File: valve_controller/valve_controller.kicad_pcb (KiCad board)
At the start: 2 copper layers, 34 parts, among them J1 643260100604, J10 643260100604, J11 643260100604, J2 T4143512051-000, J3 M12A-04PMMP-SF8001, J5 643260100604, J6 643260100604, J7 643260100604, J8 643260100604, J9 643260100604, U1 LAN8720A, U2 ADS1115IDGS, U3 MCP4728, U4 ESP32-WROOM-32, U5 LM2596S-5, U7 ADS1115IDGS, U8 MCP4728, U9 AP2112K-3.3, Y2 ASE-25.000MHZ-LC-T

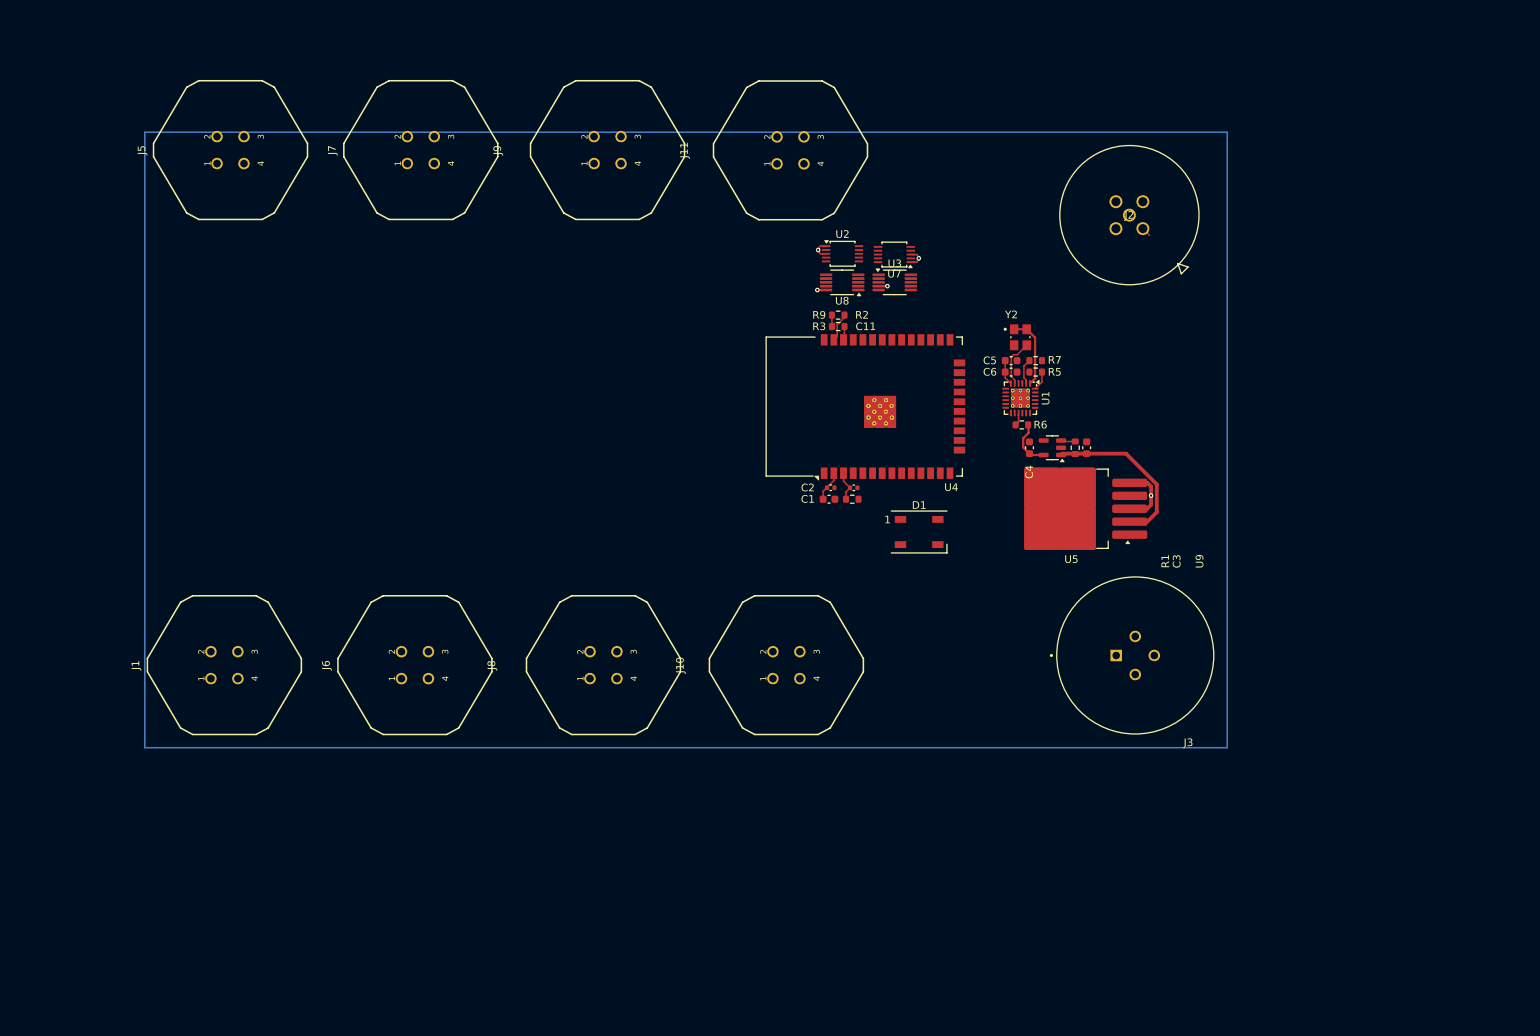
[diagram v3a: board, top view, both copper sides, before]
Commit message: Added 12v power bus
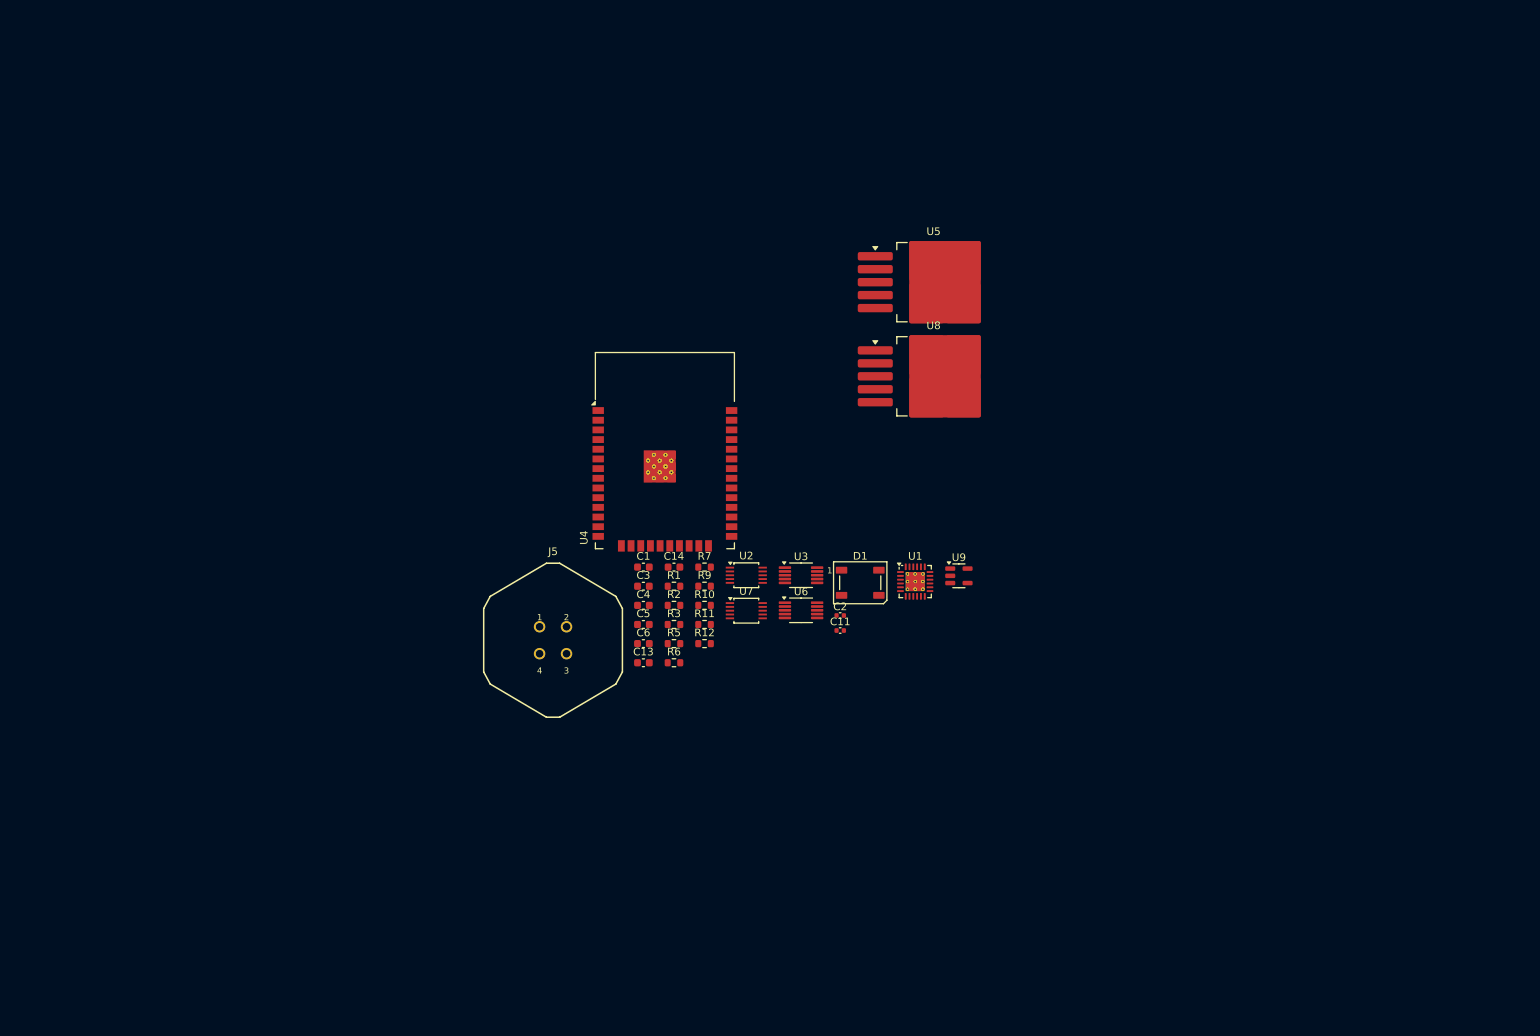
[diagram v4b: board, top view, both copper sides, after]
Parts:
- removed J1, J10, J11, J6, J7, J8, J9: 643260100604, 643260100604:643260100604
- removed J2: T4143512051-000, T4143512051_000:CONN5_T4143512051
- removed J3: M12A-04PMMP-SF8001, M12A-04PMMP-SF8001:AMPHENOL_M12A-04PMMP-SF8001
- removed Y2: ASE-25.000MHZ-LC-T, ASE-25.000MHZ-LC-T:XTAL_ASE-25.000MHZ-LC-T
- added C13: 10uF, Capacitor_SMD:C_0603_1608Metric, F.Cu at (120.5, 122.5)
- added C14: 0.1uF, Capacitor_SMD:C_0603_1608Metric, F.Cu at (124.5, 109.9)
- added R10: 10k, Resistor_SMD:R_0603_1608Metric, F.Cu at (128.5, 114.9)
- added R11: 10k, Resistor_SMD:R_0603_1608Metric, F.Cu at (128.5, 117.4)
- added R12: 100k, Resistor_SMD:R_0603_1608Metric, F.Cu at (128.5, 119.9)
- added U6: GP8403, Package_SO:MSOP-10_3x3mm_P0.5mm, F.Cu at (141.2, 115.6)
- U5: value LM2596S-5 -> LM2576S-12
- U8: value MCP4728 -> LM2576S-5; footprint Package_SO:MSOP-10_3x3mm_P0.5mm -> Package_TO_SOT_SMD:TO-263-5_TabPin3
- moved J5 77.0 mm to (108.6, 119.5), turned to 0 degrees
- moved C3 60.9 mm to (120.5, 112.4), turned to 0 degrees
- moved C6 60.0 mm to (120.5, 119.9)
- moved C5 59.4 mm to (120.5, 117.4)
- moved R5 59.3 mm to (124.5, 119.9)
- moved R1 55.7 mm to (124.5, 112.4), turned to 0 degrees
- moved R6 55.3 mm to (124.5, 122.5)
- moved C4 54.7 mm to (120.5, 114.9), turned to 0 degrees
- moved R7 51.2 mm to (128.5, 109.9)
- moved U7 50.6 mm to (134.0, 115.6), turned to 0 degrees
- moved R3 44.6 mm to (124.5, 117.4)
- moved U2 44.0 mm to (134.0, 111.0)
- moved U3 40.3 mm to (141.2, 111.0)
- moved R9 39.7 mm to (128.5, 112.4)
- moved U5 34.8 mm to (158.5, 72.5), turned to 0 degrees
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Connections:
- J5 pad 1: /AIN0_ADC0 -> +24V
- J5 pad 2: unconnected-(J5-Pad2) -> /ANOUT0_DAC0
- J5 pad 3: unconnected-(J5-Pad3) -> GND
- J5 pad 4: /ANOUT0_DAC0 -> /AIN0_ADC0
- U2 pad 1: GND -> /SCL
- U3 pad 1: +3V3 -> +5V
- U3 pad 4: GND -> /nLDAC_DAC0
- U3 pad 5: unconnected-(U3-RDY/~{BSY}-Pad5) -> /RDY_DAC0
- U4 pad 10: unconnected-(U4-IO25-Pad10) -> /RGB_LED
- U4 pad 11: unconnected-(U4-IO26-Pad11) -> /RDY_DAC0
- U4 pad 12: unconnected-(U4-IO27-Pad12) -> /nLDAC_DAC0
- U4 pad 34: unconnected-(U4-RXD0/IO3-Pad34) -> /ESP_TX
- U4 pad 35: unconnected-(U4-TXD0/IO1-Pad35) -> /ESP_RX
- U4 pad 6: unconnected-(U4-IO34-Pad6) -> /RXD1
- U4 pad 7: unconnected-(U4-IO35-Pad7) -> /RXD0
- U4 pad 8: unconnected-(U4-IO32-Pad8) -> /MDC
- U5 pad 1: +24V -> unconnected-(U5-VIN-Pad1)
- U5 pad 2: +5V -> unconnected-(U5-OUT-Pad2)
- U5 pad 3: GND -> unconnected-(U5-GND-Pad3)
- U5 pad 5: GND -> unconnected-(U5-~{ON}/OFF-Pad5)
- U7 pad 1: GND -> /SDA
- U8 pad 1: +3V3 -> unconnected-(U8-VIN-Pad1)
- U8 pad 2: /SCL -> unconnected-(U8-OUT-Pad2)
- U8 pad 3: /SDA -> unconnected-(U8-GND-Pad3)
- U8 pad 4: GND -> unconnected-(U8-FB-Pad4)
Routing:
- net +5V: track 22.0 -> 0.00 mm
- net +3V3: track 21.9 -> 0.00 mm
- net GND: track 16.3 -> 0.00 mm, vias 5 -> 0
- net /25MHZ: track 6.32 -> 0.00 mm
- net /ESP_EN: track 3.99 -> 0.00 mm
- net /SDA: track 3.82 -> 0.00 mm
- net Net-(U1-LED2/~{INTSEL}): track 3.41 -> 0.00 mm
- net Net-(U1-VDDCR): track 3.30 -> 0.00 mm
- net Net-(U1-RBIAS): track 2.55 -> 0.00 mm
- net Net-(U9-EN): track 1.91 -> 0.00 mm
- net /SCL: track 1.80 -> 0.00 mm
- net Net-(U1-~{RST}): track 1.72 -> 0.00 mm
- net unconnected-(U4-IO34-Pad6): track 0.53 -> 0.00 mm
- net /TXD0: track 0.53 -> 0.00 mm

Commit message: Layout V2
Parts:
- removed R10, R11: 10k, Resistor_SMD:R_0603_1608Metric
- removed R12, R9: 100k, Resistor_SMD:R_0603_1608Metric
- added C10: 100uF, Capacitor_SMD:C_0603_1608Metric, F.Cu at (184.5, 95.7)
- added C12: 1uF, Capacitor_SMD:C_0603_1608Metric, F.Cu at (93.1, 85.0)
- added C15: 10uF, Capacitor_SMD:C_0603_1608Metric, F.Cu at (154.9, 83.7)
- added C16: 10uF, Capacitor_SMD:C_0603_1608Metric, F.Cu at (96.1, 85.0)
- added C17: 10uF, Capacitor_SMD:C_0603_1608Metric, F.Cu at (156.4, 83.7)
- added C18: 100uF, Capacitor_SMD:C_0603_1608Metric, F.Cu at (197.6, 68.6)
- added C19: 100uF, Capacitor_SMD:C_0603_1608Metric, F.Cu at (196.7, 82.2)
- added C20: 1uF, Capacitor_SMD:C_0603_1608Metric, F.Cu at (96.4, 108.5)
- added C21: 1uF, Capacitor_SMD:C_0603_1608Metric, F.Cu at (153.3, 109.8)
- added C22: 10uF, Capacitor_SMD:C_0603_1608Metric, F.Cu at (93.4, 108.5)
- added C23: 10uF, Capacitor_SMD:C_0603_1608Metric, F.Cu at (156.2, 109.8)
- added C24: 22uF, Capacitor_SMD:C_0603_1608Metric, F.Cu at (167.1, 99.6)
- added C25: 10uF, Capacitor_SMD:C_0603_1608Metric, F.Cu at (94.9, 108.5)
- added C26: 10uF, Capacitor_SMD:C_0603_1608Metric, F.Cu at (154.8, 109.8)
- added C27: 22uF, Capacitor_SMD:C_0603_1608Metric, F.Cu at (175.9, 100.4)
- added C7: 100uF, Capacitor_SMD:C_0603_1608Metric, F.Cu at (198.4, 106.3)
- added C8: 10nF, Capacitor_SMD:C_0603_1608Metric, F.Cu at (171.8, 82.0)
- added C9: 270pF, Capacitor_SMD:C_0603_1608Metric, F.Cu at (176.4, 84.0)
- added D10: SMAJ12A, Diode_SMD:D_SMA, F.Cu at (88.8, 113.8)
- added D11: SMAJ12A, Diode_SMD:D_SMA, F.Cu at (148.7, 114.2)
- added D2: SS34, Diode_SMD:D_SMA, F.Cu at (195.9, 94.9)
- added D3: SMAJ12A, Diode_SMD:D_SMA, F.Cu at (100.8, 79.5)
- added D4: SMAJ12A, Diode_SMD:D_SMA, F.Cu at (160.6, 79.3)
- added D5: SMAJ12A, Diode_SMD:D_SMA, F.Cu at (89.0, 79.4)
- added D6: SMAJ12A, Diode_SMD:D_SMA, F.Cu at (149.3, 79.2)
- added D7: SS34, Diode_SMD:D_SMA, F.Cu at (185.3, 81.5)
- added D8: SMAJ12A, Diode_SMD:D_SMA, F.Cu at (100.5, 113.7)
- added D9: SMAJ12A, Diode_SMD:D_SMA, F.Cu at (160.1, 113.8)
- added J1: T4132512041-000, T4132512041-000:CONN4_T4132512041, F.Cu at (217.0, 66.5)
- added J10: M12A-05PFFP-SF8001, M12A_05footprints:CONN_SF8001_AMP, F.Cu at (139.4, 121.8)
- added J11: M12A-05PFFP-SF8001, M12A_05footprints:CONN_SF8001_AMP, F.Cu at (169.4, 121.8)
- added J2: 20021511-00006T4LF, 20021511_00006T4LF:AMPHENOL_20021511-00006T4LF, F.Cu at (191.9, 124.3)
- added J3: 54-00384, 54_00384:54, F.Cu at (214.4, 124.2)
- added J4: M12A-05PFFP-SF8001, M12A_05footprints:CONN_SF8001_AMP, F.Cu at (79.4, 66.8)
- added J6: M12A-05PFFP-SF8001, M12A_05footprints:CONN_SF8001_AMP, F.Cu at (139.4, 66.7)
- added J7: M12A-05PFFP-SF8001, M12A_05footprints:CONN_SF8001_AMP, F.Cu at (169.4, 66.7)
- added J8: M12A-05PFFP-SF8001, M12A_05footprints:CONN_SF8001_AMP, F.Cu at (79.4, 121.7)
- added J9: M12A-05PFFP-SF8001, M12A_05footprints:CONN_SF8001_AMP, F.Cu at (109.4, 121.7)
- added L1: SRP6530A-100M, SRP6530A_100M:IND_SRP6530A_BRN, F.Cu at (189.9, 94.5)
- added L2: SRP6530A-100M, SRP6530A_100M:IND_SRP6530A_BRN, F.Cu at (191.4, 82.0)
- added R4: 12.1k, Resistor_SMD:R_0603_1608Metric, F.Cu at (175.6, 93.4)
- added U10: GP8403-TC50-EW, GP8403:ESSOP-10_L4.9-W3.9-P1.00-LS6.0-BL-EP, F.Cu at (154.8, 102.9)
- added U11: AP2112K-3.3, Package_TO_SOT_SMD:SOT-23-5, F.Cu at (171.6, 100.4)
- added Y1: ASE-25.000MHZ-LC-T, ASE-25.000MHZ-LC-T:XTAL_ASE-25.000MHZ-LC-T, F.Cu at (175.6, 89.0)
- C11: value 0.1uF -> 100nF; footprint Capacitor_SMD:C_0402_1005Metric -> Capacitor_SMD:C_0603_1608Metric
- C13: value 10uF -> 1uF
- C14: value 0.1uF -> 10uF
- C2: footprint Capacitor_SMD:C_0402_1005Metric -> Capacitor_SMD:C_0603_1608Metric
- C3: value 22uF -> 0.1uF
- C4: value 22uF -> 10nF
- C5: value 1uF -> 22nF
- C6: value 470pF -> 1uF
- J5: value 643260100604 -> M12A-05PFFP-SF8001; footprint 643260100604:643260100604 -> M12A_05footprints:CONN_SF8001_AMP
- R1, R3: value 100k -> 10k
- R5: value 12.1k -> 100k
- R6, R7: value 10k -> 100k
- U2: value ADS1115IDGS -> ESP32-WROOM-32; footprint Package_SO:TSSOP-10_3x3mm_P0.5mm -> RF_Module:ESP32-WROOM-32
- U3: value MCP4728 -> LM2576S-12; footprint Package_SO:MSOP-10_3x3mm_P0.5mm -> Package_TO_SOT_SMD:TO-263-5_TabPin3
- U4: value ESP32-WROOM-32 -> ADS1115IDGS; footprint RF_Module:ESP32-WROOM-32 -> Package_SO:TSSOP-10_3x3mm_P0.5mm
- U5: value LM2576S-12 -> GP8403-TC50-EW; footprint Package_TO_SOT_SMD:TO-263-5_TabPin3 -> GP8403:ESSOP-10_L4.9-W3.9-P1.00-LS6.0-BL-EP
- U6: value GP8403 -> GP8403-TC50-EW; footprint Package_SO:MSOP-10_3x3mm_P0.5mm -> GP8403:ESSOP-10_L4.9-W3.9-P1.00-LS6.0-BL-EP
- U9: value AP2112K-3.3 -> GP8403-TC50-EW; footprint Package_TO_SOT_SMD:SOT-23-5 -> GP8403:ESSOP-10_L4.9-W3.9-P1.00-LS6.0-BL-EP
- moved C1 109.1 mm to (226.9, 85.8)
- moved C3 104.8 mm to (221.9, 85.8), turned to 180 degrees
- moved R2 102.1 mm to (221.9, 84.3)
- moved R6 101.9 mm to (225.3, 108.0)
- moved R5 101.4 mm to (225.3, 109.5)
- moved C2 86.7 mm to (226.9, 84.3)
- moved U2 86.5 mm to (219.3, 96.8), turned to -90 degrees
- moved U9 67.6 mm to (94.8, 102.3), turned to 180 degrees
- moved U5 66.5 mm to (94.7, 90.8)
- moved C6 64.9 mm to (174.4, 84.0), turned to -90 degrees
- moved C5 61.5 mm to (171.8, 83.5), turned to 180 degrees
- moved C4 59.4 mm to (171.8, 85.0), turned to 180 degrees
- moved R3 57.1 mm to (175.6, 92.0)
- moved J5 52.8 mm to (109.4, 66.7)
- moved C13 50.9 mm to (153.5, 83.7), turned to -90 degrees
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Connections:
- C11 pad 1: /ESP_EN -> +3V3
- C13 pad 2: +5V -> Net-(U6-V5V)
- C14 pad 2: +5V -> /AOUT1_DAC0
- C3 pad 1: +5V -> /ESP_EN
- C4 pad 1: +3V3 -> GND
- C4 pad 2: GND -> +3V3
- C5 pad 1: Net-(U1-VDDCR) -> GND
- C5 pad 2: GND -> +3V3
- C6 pad 1: Net-(U1-VDDCR) -> GND
- C6 pad 2: GND -> Net-(U1-VDDCR)
- J5 pad 2: /ANOUT0_DAC0 -> /AOUT1_DAC0
- J5 pad 4: /AIN0_ADC0 -> /AIN1_ADC0
- R1 pad 1: Net-(U9-EN) -> Net-(U1-~{RST})
- R1 pad 2: +5V -> +3V3
- R3 pad 1: +3V3 -> Net-(U1-LED2/~{INTSEL})
- R3 pad 2: /SCL -> GND
- R5 pad 1: GND -> +3V3
- R5 pad 2: Net-(U1-RBIAS) -> /SCL
- R6 pad 1: Net-(U1-~{RST}) -> +3V3
- R6 pad 2: +3V3 -> /SDA
- R7 pad 1: Net-(U1-LED2/~{INTSEL}) -> Net-(U11-EN)
- R7 pad 2: GND -> +5V
- U1 pad 14: /REF_CLK -> /ESP_IO0
- U2 pad 1: /SCL -> GND
- U2 pad 10: /SCL -> /RGB_LED
- U2 pad 2: unconnected-(U2-ALERT/RDY-Pad2) -> +3V3
- U2 pad 3: GND -> /ESP_EN
- U2 pad 4: /AIN0_ADC0 -> unconnected-(U2-SENSOR_VP-Pad4)
- U2 pad 5: /AIN1_ADC0 -> unconnected-(U2-SENSOR_VN-Pad5)
- U2 pad 6: /AIN2_ADC0 -> /RXD1
- U2 pad 7: /AIN3_ADC0 -> /RXD0
- U2 pad 8: +3V3 -> /MDC
- U2 pad 9: /SDA -> unconnected-(U2-IO33-Pad9)
- U3 pad 1: +5V -> +24V
- U3 pad 2: /SCL -> Net-(D2-K)
- U3 pad 3: /SDA -> GND
- U3 pad 4: /nLDAC_DAC0 -> +12V
- U3 pad 5: /RDY_DAC0 -> GND
- U4 pad 1: GND -> /SCL
- U4 pad 10: /RGB_LED -> /SCL
- U4 pad 2: +3V3 -> unconnected-(U4-ALERT/RDY-Pad2)
- U4 pad 3: /ESP_EN -> GND
- U4 pad 4: unconnected-(U4-SENSOR_VP-Pad4) -> /AIN0_ADC0
- U4 pad 5: unconnected-(U4-SENSOR_VN-Pad5) -> /AIN1_ADC0
- U4 pad 6: /RXD1 -> /AIN2_ADC0
- U4 pad 7: /RXD0 -> /AIN3_ADC0
- U4 pad 8: /MDC -> +3V3
- U4 pad 9: unconnected-(U4-IO33-Pad9) -> /SDA
- U5 pad 1: unconnected-(U5-VIN-Pad1) -> /SCL
- U5 pad 2: unconnected-(U5-OUT-Pad2) -> /SDA
- U5 pad 3: unconnected-(U5-GND-Pad3) -> GND
- U5 pad 4: unconnected-(U5-FB-Pad4) -> GND
- U5 pad 5: unconnected-(U5-~{ON}/OFF-Pad5) -> +12V
- U6 pad 1: unconnected-(U6-VDD-Pad1) -> /SCL
- U6 pad 10: unconnected-(U6-VSS-Pad10) -> Net-(U6-V5V)
- U6 pad 2: unconnected-(U6-SCL-Pad2) -> /SDA
- U6 pad 3: unconnected-(U6-SDA-Pad3) -> +3V3
- U6 pad 4: unconnected-(U6-~{LDAC}-Pad4) -> GND
- U6 pad 5: unconnected-(U6-RDY/~{BSY}-Pad5) -> +12V
- U6 pad 6: unconnected-(U6-VOUTA-Pad6) -> GND
- U6 pad 7: unconnected-(U6-VOUTB-Pad7) -> /AOUT1_DAC1
- U6 pad 8: unconnected-(U6-VOUTC-Pad8) -> /AOUT0_DAC1
- U6 pad 9: unconnected-(U6-VOUTD-Pad9) -> +3V3
- U8 pad 1: unconnected-(U8-VIN-Pad1) -> +24V
- U8 pad 2: unconnected-(U8-OUT-Pad2) -> Net-(D7-K)
- U8 pad 3: unconnected-(U8-GND-Pad3) -> GND
- U8 pad 4: unconnected-(U8-FB-Pad4) -> +5V
- U8 pad 5: unconnected-(U8-~{ON}/OFF-Pad5) -> GND
- U9 pad 1: +5V -> /SCL
- U9 pad 2: GND -> /SDA
- U9 pad 3: Net-(U9-EN) -> GND
- U9 pad 4: unconnected-(U9-NC-Pad4) -> +3V3
- U9 pad 5: +3V3 -> +12V
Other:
- board outline added: 166.5 x 85 mm
- copper layers 2 -> 4

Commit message: Routing V1
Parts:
- added REF0: MountingHole_2.5mm, MountingHole:MountingHole_2.5mm, F.Cu at (69.4, 59.2)
- added REF1: MountingHole_2.5mm, MountingHole:MountingHole_2.5mm, F.Cu at (69.4, 134.3)
- added REF2: MountingHole_2.5mm, MountingHole:MountingHole_2.5mm, F.Cu at (231.1, 134.3)
- added REF3: MountingHole_2.5mm, MountingHole:MountingHole_2.5mm, F.Cu at (231.1, 59.2)
- moved C27 21.1 mm to (195.3, 92.0)
- moved C24 21.1 mm to (186.4, 91.1)
- moved R7 21.1 mm to (186.4, 92.6)
- moved U11 21.1 mm to (191.0, 92.0)
- moved R5 10.3 mm to (215.0, 109.3)
- moved R6 10.3 mm to (215.0, 107.8)
- moved D2 6.48 mm to (196.5, 101.4)
- moved L1 6.48 mm to (190.5, 101.0)
- moved U3 6.48 mm to (192.2, 116.6)
- moved C10 6.48 mm to (185.1, 102.1)
- moved C7 6.48 mm to (199.0, 112.7)
- moved D1 5.05 mm to (172.8, 103.5)
- moved J7 5.00 mm to (169.4, 71.7), turned to 180 degrees
- moved J2 3.60 mm to (191.9, 127.9)
- moved C21 2.97 mm to (156.2, 109.8)
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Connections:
- U2 pad 10: /RGB_LED -> /RXER
- U2 pad 11: /RDY_DAC0 -> unconnected-(U2-IO26-Pad11)
- U2 pad 12: /nLDAC_DAC0 -> /RXD0
- U2 pad 13: /TXD0 -> /RXD1
- U2 pad 14: /TXEN -> /MDIO
- U2 pad 16: /TXD1 -> /TXD0
- U2 pad 23: /MDIO -> unconnected-(U2-IO15-Pad23)
- U2 pad 24: /CRS_DV -> /RGB_LED
- U2 pad 26: /RXER -> unconnected-(U2-IO4-Pad26)
- U2 pad 27: unconnected-(U2-IO16-Pad27) -> /SCL
- U2 pad 28: unconnected-(U2-IO17-Pad28) -> /SDA
- U2 pad 36: /SCL -> unconnected-(U2-IO22-Pad36)
- U2 pad 37: /SDA -> unconnected-(U2-IO23-Pad37)
- U2 pad 6: /RXD1 -> /TXD1
- U2 pad 7: /RXD0 -> /TXEN
- U2 pad 9: unconnected-(U2-IO33-Pad9) -> /CRS_DV
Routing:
- net /SCL: track 0.00 -> 213.4 mm, vias 0 -> 7
- net /SDA: track 0.00 -> 202.9 mm, vias 0 -> 7
- net +12V: track 0.00 -> 127.0 mm
- net /ESP_EN: track 0.00 -> 103.5 mm
- net /ESP_IO0: track 0.00 -> 86.0 mm, vias 0 -> 2
- net /RGB_LED: track 0.00 -> 81.3 mm
- net +3V3: track 0.00 -> 73.3 mm, vias 0 -> 20
- net /TX_P: track 0.00 -> 69.2 mm, vias 0 -> 2
- net /RX_P: track 0.00 -> 65.8 mm, vias 0 -> 2
- net +24V: track 0.00 -> 65.4 mm, vias 0 -> 11
- net /ESP_TX: track 0.00 -> 62.2 mm
- net /TX_N: track 0.00 -> 61.4 mm, vias 0 -> 2
- net /RX_N: track 0.00 -> 60.7 mm, vias 0 -> 2
- net /TXD1: track 0.00 -> 60.5 mm, vias 0 -> 2
- net /AOUT1_DAC2: track 0.00 -> 59.4 mm, vias 0 -> 2
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- added copper zone on In1.Cu, net +24V
- added copper zone on In1.Cu, net +3V3
- added copper zone on In2.Cu, net GND
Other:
- board size 166.5 x 85 mm -> 171.6 x 85 mm

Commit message: LED + routing V2
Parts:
- added D12: WS2812B, LED_SMD:LED_WS2812B_PLCC4_5.0x5.0mm_P3.2mm, F.Cu at (169.4, 81.7)
- added D13: WS2812B, LED_SMD:LED_WS2812B_PLCC4_5.0x5.0mm_P3.2mm, F.Cu at (139.4, 81.7)
- added D14: WS2812B, LED_SMD:LED_WS2812B_PLCC4_5.0x5.0mm_P3.2mm, F.Cu at (109.4, 81.7)
- added D15: WS2812B, LED_SMD:LED_WS2812B_PLCC4_5.0x5.0mm_P3.2mm, F.Cu at (79.4, 81.7)
- added D16: WS2812B, LED_SMD:LED_WS2812B_PLCC4_5.0x5.0mm_P3.2mm, F.Cu at (79.4, 111.7)
- added D17: WS2812B, LED_SMD:LED_WS2812B_PLCC4_5.0x5.0mm_P3.2mm, F.Cu at (109.4, 111.7)
- added D18: WS2812B, LED_SMD:LED_WS2812B_PLCC4_5.0x5.0mm_P3.2mm, F.Cu at (139.4, 111.8)
- added D19: WS2812B, LED_SMD:LED_WS2812B_PLCC4_5.0x5.0mm_P3.2mm, F.Cu at (169.4, 111.8)
- added D20: WL-SMCW_0603, 150060VS75000:WL-SMCW_0603, F.Cu at (217.2, 111.8)
- added D21: WL-SMCW_0603, 150060VS75000:WL-SMCW_0603, F.Cu at (211.6, 111.8)
- added D22: WL-SMCW_0603, 150060VS75000:WL-SMCW_0603, F.Cu at (214.4, 81.7)
- added R8: 270, Resistor_SMD:R_0603_1608Metric, F.Cu at (211.6, 109.1)
- added R9: 10k, Resistor_SMD:R_0603_1608Metric, F.Cu at (208.6, 109.1)
- R3: value 10k -> 270
- moved R3 45.0 mm to (217.3, 109.1)
- moved D1 38.6 mm to (202.2, 78.5), turned to -90 degrees
- moved C11 11.0 mm to (177.7, 99.9)
- moved C4 11.0 mm to (170.7, 94.7)
- moved C5 11.0 mm to (170.7, 93.2)
- moved C6 11.0 mm to (173.4, 95.0)
- moved C8 11.0 mm to (170.7, 91.7)
- moved C9 11.0 mm to (175.4, 95.0)
- moved R1 11.0 mm to (164.9, 100.2)
- moved R4 11.0 mm to (174.6, 104.6)
- moved U1 11.0 mm to (169.6, 99.5)
- moved Y1 11.0 mm to (174.6, 100.0)
- moved D9 8.15 mm to (156.7, 121.2)
- moved D11 7.79 mm to (152.2, 121.2)
- moved D8 7.44 mm to (96.8, 120.1), turned to 90 degrees
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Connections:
- D1 pad 2: unconnected-(D1-DOUT-Pad2) -> /LED_01
- R3 pad 1: Net-(U1-LED2/~{INTSEL}) -> Net-(D20-Pad1)
- U1 pad 2: Net-(U1-LED2/~{INTSEL}) -> /LED2
- U1 pad 3: unconnected-(U1-LED1/REGOFF-Pad3) -> /LED1
- U2 pad 11: unconnected-(U2-IO26-Pad11) -> /RGB_LED
- U2 pad 24: /RGB_LED -> unconnected-(U2-IO2-Pad24)
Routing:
- net GND: track 3.96 -> 117.0 mm, vias 65 -> 52
- net /RGB_LED: track 81.3 -> 16.1 mm
- net /LED2: track 0.00 -> 51.6 mm
- net /LED1: track 0.00 -> 50.9 mm, vias 0 -> 2
- net /LED_45: track 0.00 -> 32.7 mm
- net /LED_01: track 0.00 -> 30.3 mm, vias 0 -> 2
- net /AOUT1_DAC2: track 59.4 -> 31.2 mm, vias 2 -> 0
- net /LED_23: track 0.00 -> 26.5 mm, vias 0 -> 2
- net /LED_67: track 0.00 -> 26.5 mm, vias 0 -> 2
- net /LED_56: track 0.00 -> 26.5 mm, vias 0 -> 2
- net /LED_78: track 0.00 -> 26.5 mm, vias 0 -> 2
- net /LED_12: track 0.00 -> 26.5 mm, vias 0 -> 2
- net /LED_34: track 0.00 -> 26.5 mm, vias 0 -> 2
- net +24V: track 65.4 -> 43.6 mm, vias 11 -> 1
- net /ESP_EN: track 103.5 -> 83.3 mm, vias 0 -> 1
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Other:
- outline, holes or cut-outs redrawn

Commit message: tweaks for case
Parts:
- removed REF0, REF1, REF2, REF3: MountingHole_2.5mm, MountingHole:MountingHole_2.5mm
- added ?: , , F.Cu at (69.1, 134.6)
- added ?: , , F.Cu at (139.8, 92.2)
- added ?: , , F.Cu at (139.6, 103.0)
- added R10: 1k, Resistor_SMD:R_0603_1608Metric, F.Cu at (217.9, 81.7)
- added REF**: MountingHole_2.2mm_M2_DIN965_Pad, MountingHole:MountingHole_2.2mm_M2_DIN965_Pad, F.Cu at (231.4, 134.6)
- added REF**: MountingHole_2.2mm_M2_DIN965_Pad, MountingHole:MountingHole_2.2mm_M2_DIN965_Pad, F.Cu at (231.4, 58.9)
- added REF**: MountingHole_2.2mm_M2_DIN965_Pad, MountingHole:MountingHole_2.2mm_M2_DIN965_Pad, F.Cu at (69.1, 134.6)
- added REF**: MountingHole_2.2mm_M2_DIN965_Pad, MountingHole:MountingHole_2.2mm_M2_DIN965_Pad, F.Cu at (139.6, 103.0)
- added REF**: MountingHole_2.2mm_M2_DIN965_Pad, MountingHole:MountingHole_2.2mm_M2_DIN965_Pad, F.Cu at (69.1, 58.9)
- added REF**: MountingHole_2.2mm_M2_DIN965_Pad, MountingHole:MountingHole_2.2mm_M2_DIN965_Pad, F.Cu at (139.8, 92.2)
- moved D12 2.50 mm to (169.4, 84.2)
- moved D13 2.50 mm to (139.4, 84.2)
- moved D15 2.50 mm to (79.4, 84.2)
- moved D16 2.50 mm to (79.4, 109.2)
- moved D17 2.50 mm to (109.4, 109.2)
- moved D18 2.50 mm to (139.4, 109.2)
- moved D19 2.50 mm to (169.4, 109.3)
- moved D14 2.50 mm to (109.4, 84.2)
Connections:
- D22 pad 1: unconnected-(D22-Pad1) -> GND
- D22 pad 2: unconnected-(D22-Pad2) -> Net-(D22-Pad2)
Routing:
- net +24V: track 43.6 -> 55.5 mm
- net /LED_45: track 32.7 -> 26.6 mm
- net +12V: track 135.6 -> 133.7 mm
- net Net-(D22-Pad2): track 0.00 -> 1.81 mm
- net GND: track 117.0 -> 118.4 mm, vias 52 -> 53
- net /LED_01: track 30.3 -> 31.3 mm
- net /TXD1: track 79.4 -> 79.9 mm
